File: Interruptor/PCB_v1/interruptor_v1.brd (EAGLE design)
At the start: 100 x 80 mm, 31 parts, among them IC1 LM1117MPX-3.3, SW1 CI-11, U2 TCLD1000, X1 MAB5SH

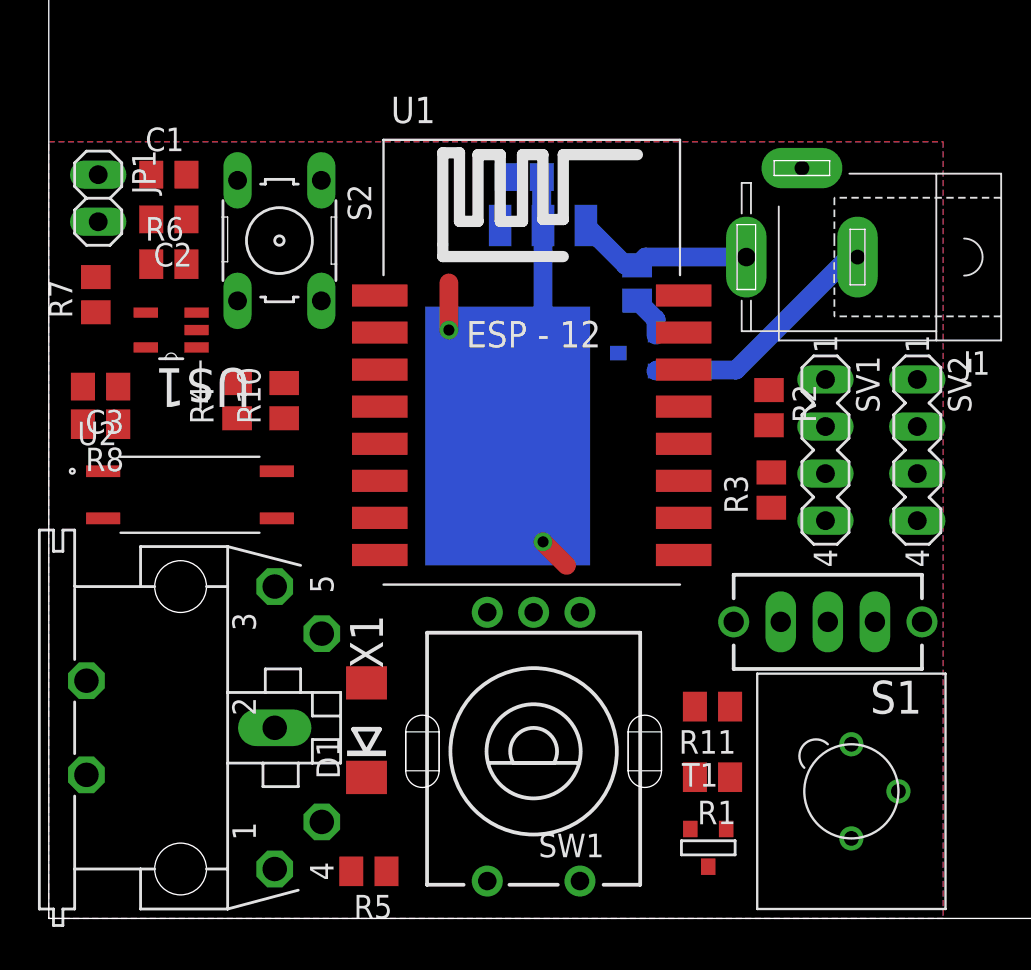
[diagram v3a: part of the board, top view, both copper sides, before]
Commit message: No DRC errors other than drill sizes, routed
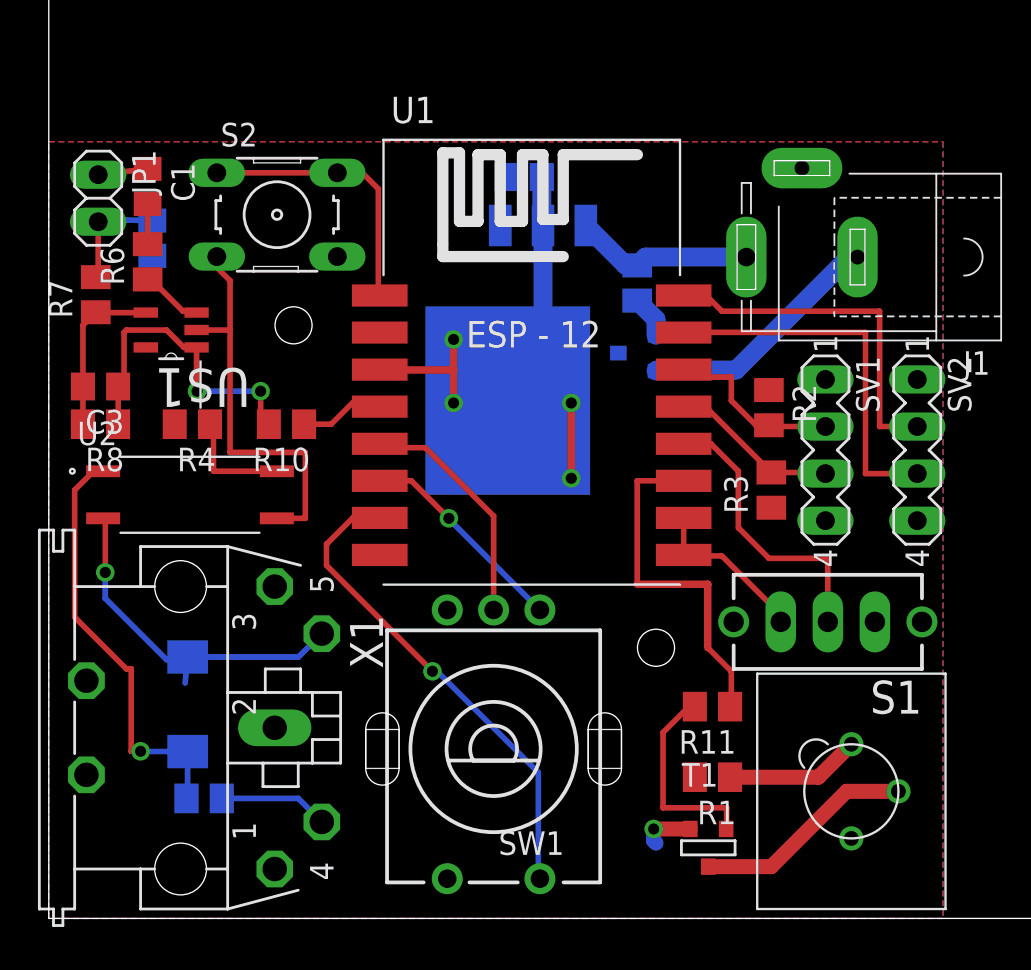
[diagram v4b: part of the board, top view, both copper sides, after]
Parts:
- moved D1 9.75 mm to (7.49, 11.6), flipped to the bottom
- moved R5 9.72 mm to (8.38, 6.48), flipped to the bottom
- moved R4 2.73 mm to (7.75, 26.7), turned to 180 degrees
- moved SW1 2.16 mm to (24.0, 9.14)
- moved S2 1.40 mm to (12.3, 38.0), turned to 0 degrees
- moved C2 1.35 mm to (5.59, 36.7), flipped to the bottom, turned to 90 degrees
- moved C1 1.31 mm to (5.33, 39.5), turned to 270 degrees
- moved R10 1.28 mm to (12.8, 26.7), turned to 180 degrees
- moved R6 1.15 mm to (5.33, 35.4), turned to 90 degrees
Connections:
- net GND: now also U$2.CASE
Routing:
- net GND: track 0.00 -> 33.6 mm, vias 0 -> 1
- net N$5: track 0.00 -> 26.4 mm, vias 0 -> 1
- net N$3: track 0.00 -> 23.1 mm, vias 0 -> 1
- net RX: track 0.00 -> 20.2 mm
- net N$4: track 0.00 -> 19.5 mm, vias 0 -> 1
- net TX: track 0.00 -> 19.2 mm
- net ESP_TRIG_OUT: track 0.00 -> 19.1 mm
- net N$12: track 0.60 -> 17.6 mm, vias 0 -> 2
- net PGM: track 0.00 -> 15.6 mm
- net N$15: track 0.00 -> 14.9 mm
- net N$13: track 0.00 -> 12.8 mm
- net N$14: track 0.00 -> 11.9 mm
- net N$11: track 0.00 -> 11.5 mm, vias 0 -> 1
- net N$21: track 0.00 -> 11.0 mm
- net SCL: track 0.00 -> 9.66 mm
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
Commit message: Fixed small alignment error and board edge
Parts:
- moved R3 0.13 mm to (38.9, 23.1)
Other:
- board size 100 x 80 mm -> 49.8 x 43.2 mm
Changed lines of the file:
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@@
 <board>
 <plain>
-<wire x1="0" y1="0" x2="100" y2="0" width="0" layer="20"/>
-<wire x1="100" y1="0" x2="100" y2="80" width="0" layer="20"/>
-<wire x1="100" y1="80" x2="0" y2="80" width="0" layer="20"/>
-<wire x1="0" y1="80" x2="0" y2="0" width="0" layer="20"/>
+<wire x1="0" y1="0" x2="49.835" y2="0" width="0" layer="20"/>
+<wire x1="49.835" y1="0" x2="49.835" y2="43.17" width="0" layer="20"/>
+<wire x1="49.835" y1="43.17" x2="0" y2="43.17" width="0" layer="20"/>
+<wire x1="0" y1="43.17" x2="0" y2="0" width="0" layer="20"/>
 <rectangle x1="20.32" y1="22.86" x2="29.21" y2="33.02" layer="16"/>
 <hole x="13.208" y="32.004" drill="2"/>
@@
 </element>
 <element name="R2" library="resistor" package="M0805" value="4.7k" x="38.862" y="27.559" rot="R270"/>
-<element name="R3" library="resistor" package="M0805" value="4.7k" x="38.989" y="23.114" rot="R90"/>
+<element name="R3" library="resistor" package="M0805" value="4.7k" x="38.862" y="23.114" rot="R90"/>
 <element name="R4" library="resistor" package="M0805" value="" x="7.747" y="26.67" rot="R180"/>
 <element name="R5" library="resistor" package="M0805" value="220" x="8.382" y="6.477" rot="MR180"/>
@@
 <contactref element="R3" pad="2"/>
 <wire x1="34.262" y1="27.613" x2="35.44" y2="27.613" width="0.3048" layer="1"/>
-<wire x1="35.44" y1="27.613" x2="38.989" y2="24.064" width="0.3048" layer="1"/>
-<wire x1="38.989" y1="24.064" x2="41.849" y2="24.064" width="0.3048" layer="1"/>
+<wire x1="35.44" y1="27.613" x2="38.862" y2="24.064" width="0.3048" layer="1"/>
+<wire x1="38.862" y1="24.064" x2="41.849" y2="24.064" width="0.3048" layer="1"/>
 <wire x1="41.849" y1="24.064" x2="41.91" y2="24.003" width="0.3048" layer="1"/>
 </signal>

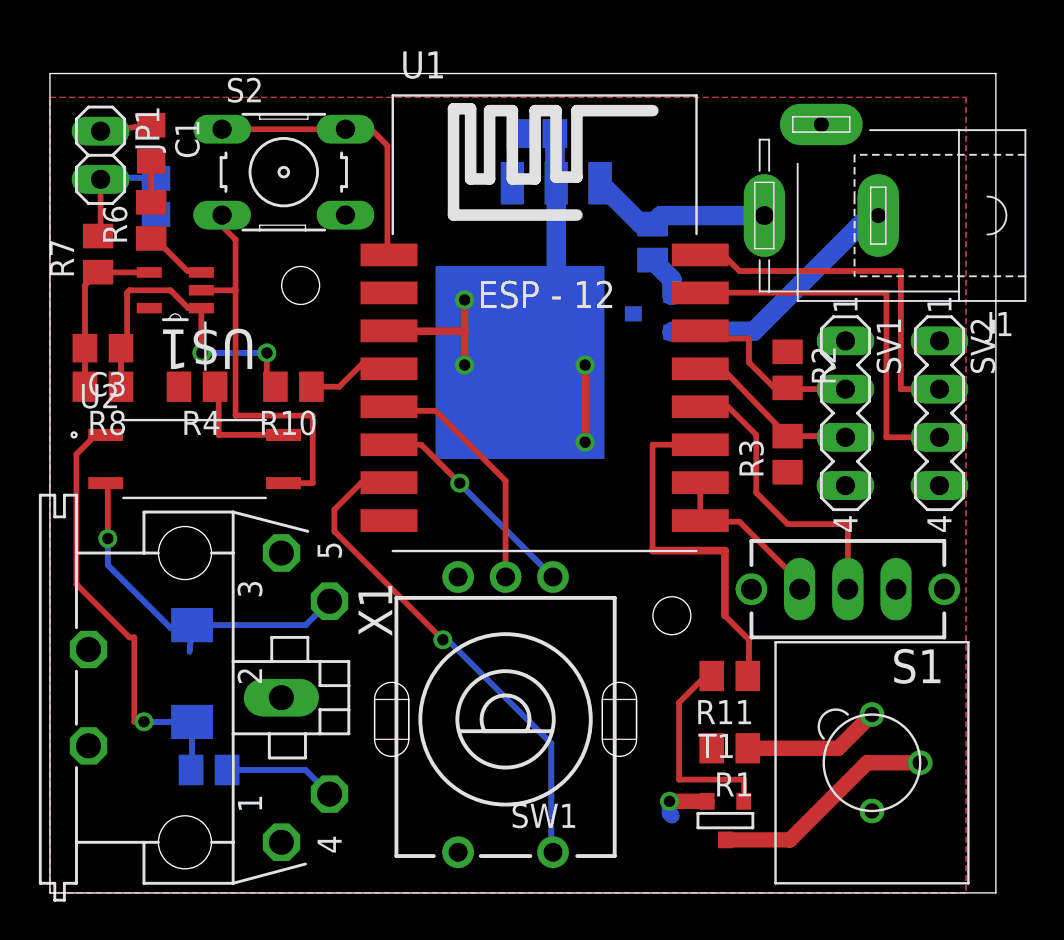
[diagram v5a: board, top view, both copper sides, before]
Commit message: placed tname/bname silkscreen
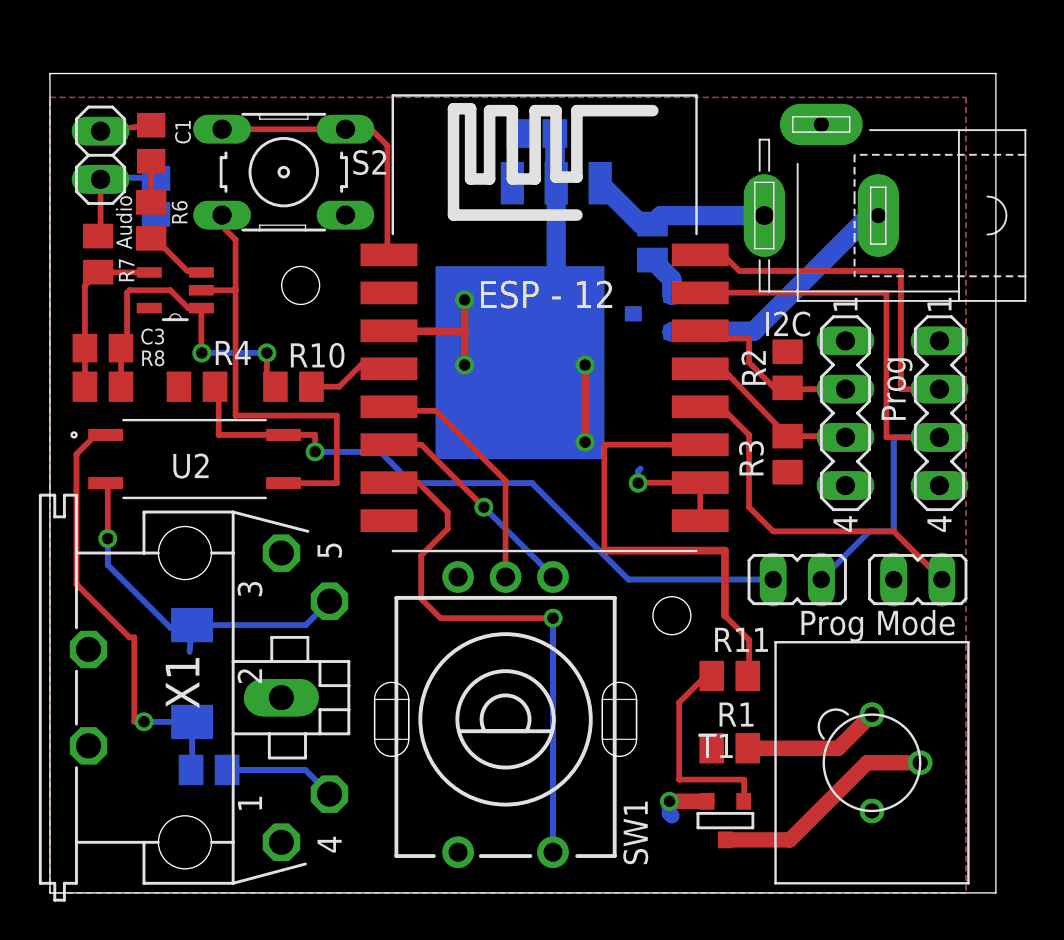
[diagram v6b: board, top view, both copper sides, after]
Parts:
- removed S1: Prog, switch:TL3XYO
- added JP2, JP3: (no value), jumper:JP1
- R4: value (none) -> 2.2k
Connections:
- net GND: now also JP3.2; no longer S1.3
- net N$1: now also JP2.1
- net PGM: now also JP3.1; no longer S1.2
- net RX: now also JP2.2
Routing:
- net N$1: track 6.15 -> 35.6 mm, vias 0 -> 1
- net RX: track 20.2 -> 32.5 mm
- net ESP_TRIG_OUT: track 19.1 -> 24.1 mm
- net PGM: track 15.6 -> 18.7 mm
- net N$5: track 26.4 -> 28.6 mm
- net GND: track 33.6 -> 33.3 mm, vias 1 -> 2
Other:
- board text added: "Audio"
- board text added: "I2C"
- board text added: "Prog"
- board text added: "Prog Mode"
